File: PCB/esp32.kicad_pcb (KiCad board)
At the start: 2 copper layers, 44 x 80.5 mm, 101 parts, among them J1 USB_C, J15 SPI_0, J16 SPI_1, J3 A0, J4 A1, J5 A2, J6 D0, J7 D1, J8 USB_VOUT, Q10 AO3400A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

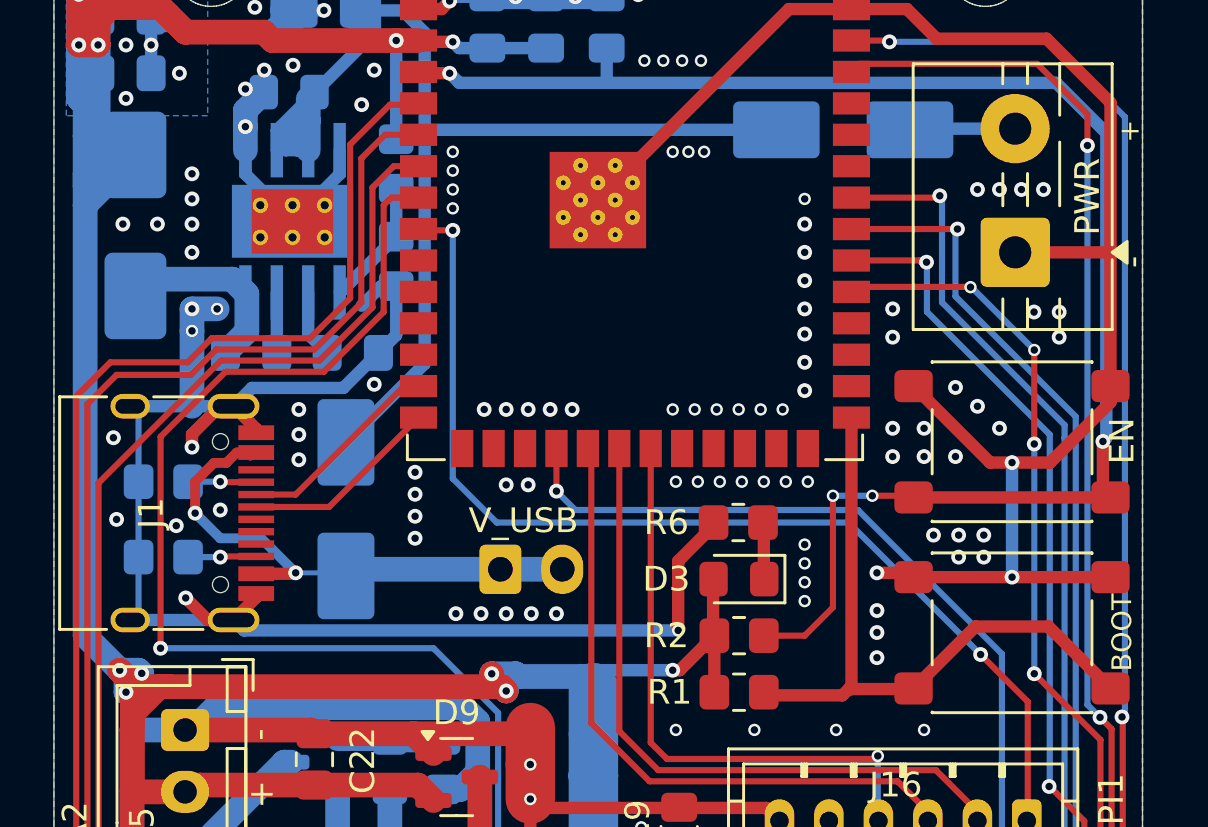
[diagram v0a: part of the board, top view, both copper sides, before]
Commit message: fix usb differential pair
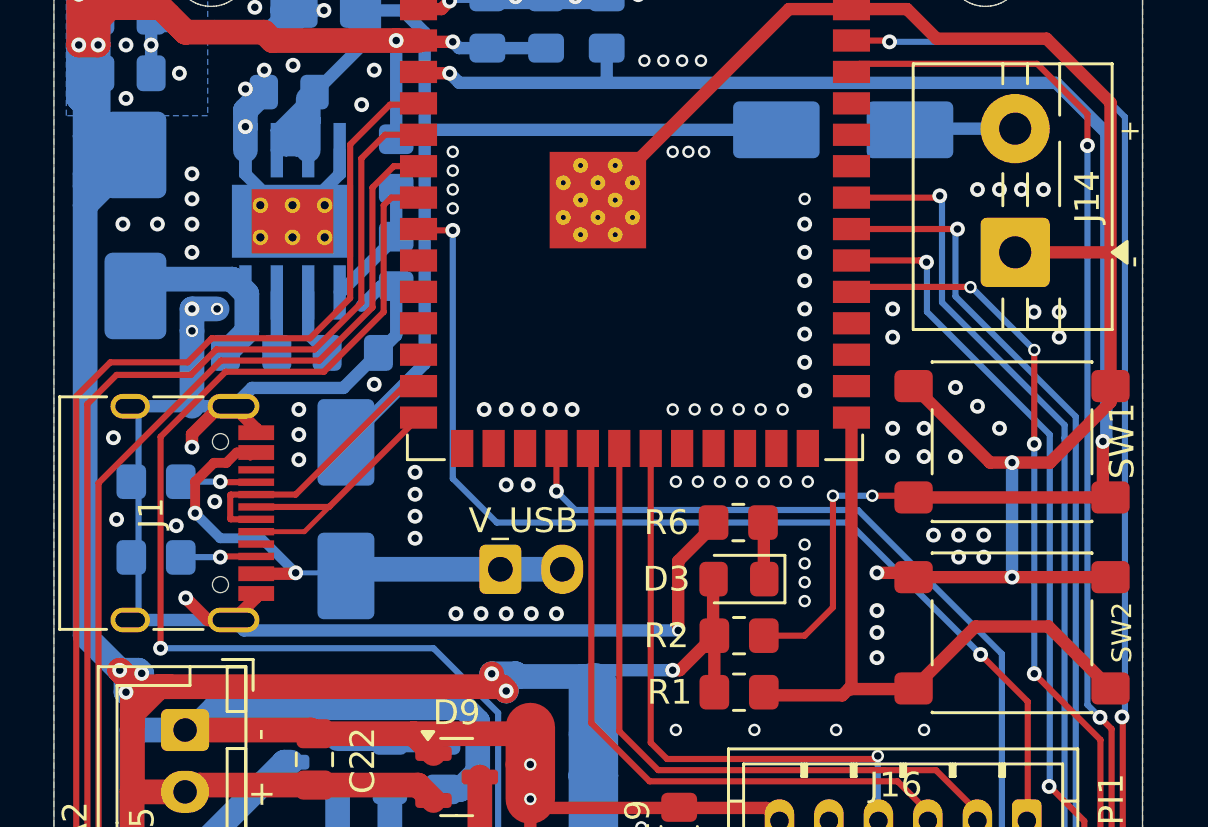
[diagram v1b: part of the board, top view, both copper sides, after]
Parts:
- moved R4 0.30 mm to (75.0, 94.5)
- moved R3 0.30 mm to (75.0, 91.4)
- renumbered PWR to J14, EN to SW1, BOOT to SW2
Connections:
- J1 pad A7: unconnected-(J1-D--PadA7) -> /D-
- J1 pad B6: unconnected-(J1-D+-PadB6) -> /D+
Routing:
- net /D+: track 8.06 -> 11.4 mm
- net /D-: track 8.38 -> 11.5 mm
